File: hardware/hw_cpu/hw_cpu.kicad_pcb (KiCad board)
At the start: 2 copper layers, 85.7 x 40.6 mm, 60 parts, among them CON1 SD_Card, IC1 MT48LC4M16A2P, J1 USB_OTG, P1 COM_EXP, P2 IO_EXP, P3 DEBUG, Q1 BC849, SW1 RESET, U2 STM32F429ZGTx, Y1 8MHz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

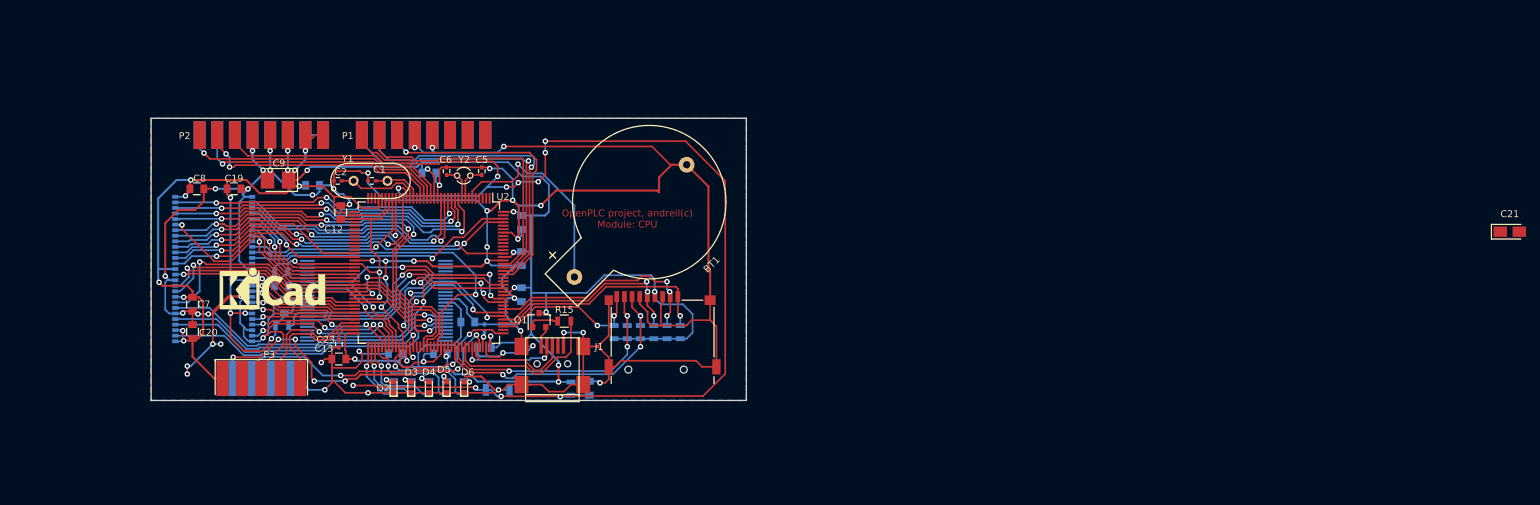
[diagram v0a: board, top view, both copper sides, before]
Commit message: Обновлена схема CPU
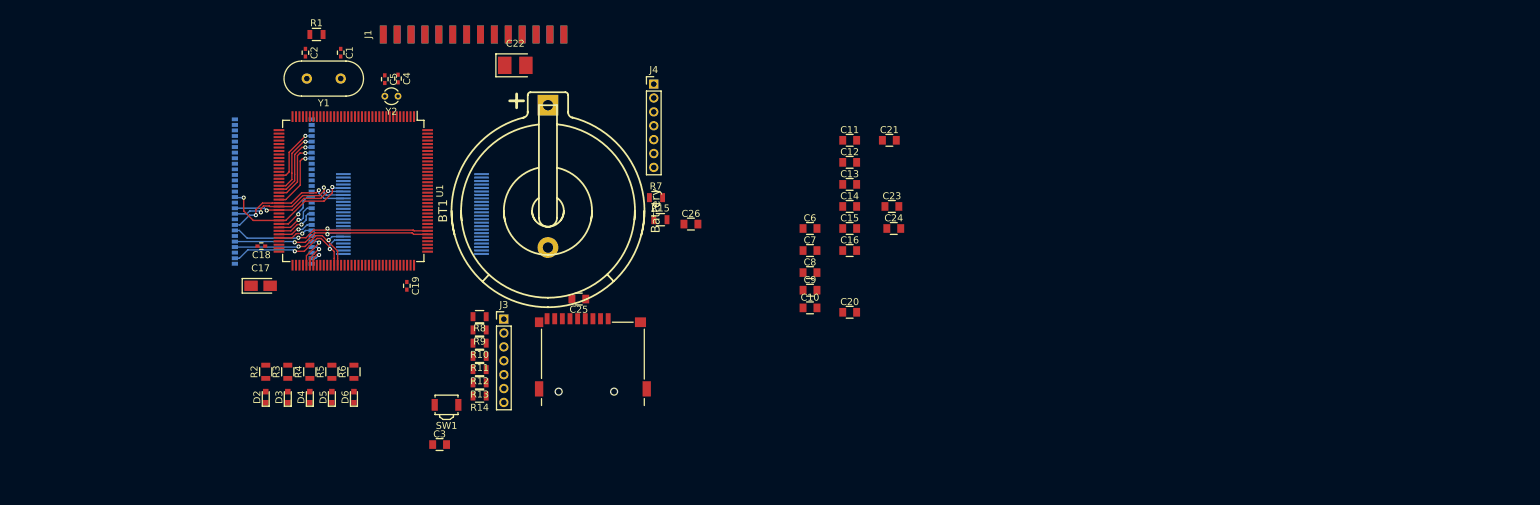
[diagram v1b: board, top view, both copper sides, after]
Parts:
- removed ??1: K9F5608, Housings_SSOP:TSOP-I-48_12x18.4mm_Pitch0.5mm
- removed P1: COM_EXP, andreil:IDC_Header_SMD_16pins
- removed P2: IO_EXP, andreil:IDC_Header_SMD_16pins
- removed P3: DEBUG, Connect:DB9F_CI
- removed Q1: BC849, TO_SOT_Packages_SMD:SOT-23
- removed REF***: KiCad-Logo_6mm_SilkScreen, Symbols:KiCad-Logo_6mm_SilkScreen
- removed the U2 at (114.3, 107.3)
- added J3: SDIO_DEB, Pin_Headers:Pin_Header_Straight_1x07_Pitch2.00mm, F.Cu at (125.1, 114.0)
- added J4: DEBUG, Pin_Headers:Pin_Header_Straight_1x07_Pitch2.00mm, F.Cu at (146.7, 80.2)
- added U1: STM32F429ZGTx, Housings_QFP:LQFP-144_20x20mm_Pitch0.5mm, F.Cu at (103.4, 95.6)
- added U3: K9F5608, Housings_SSOP:TSOP-I-48_12x18.4mm_Pitch0.5mm, B.Cu at (111.9, 98.9)
- BT1: footprint Connect:CR2032H -> w_battery_holders:keystone_1025
- C10, C11, C14, C15, C16, C24, C25, C26, C3, R1, R10, R11, R12, R13, R14, R2, R3, R4, R5, R6, R7, R8, R9, SW1: moved to F.Cu
- C17: value 100n -> 4,7u 10v; footprint Capacitors_SMD:C_0805 -> Capacitors_Tantalum_SMD:CP_Tantalum_Case-A_EIA-3216-18_Reflow; moved to F.Cu
- C18: value 100n -> 2,2u; footprint Capacitors_SMD:C_0805 -> Capacitors_SMD:C_0402; moved to F.Cu
- C19: value 100n -> 2,2u; footprint Capacitors_SMD:C_0805 -> Capacitors_SMD:C_0402
- C21: value 4,7u 10v -> 100n; footprint Capacitors_Tantalum_SMD:CP_Tantalum_Case-A_EIA-3216-18_Reflow -> Capacitors_SMD:C_0805
- C22: value 2,2u -> 4,7u 10v; footprint Capacitors_SMD:C_0402 -> Capacitors_Tantalum_SMD:CP_Tantalum_Case-B_EIA-3528-21_Reflow; moved to F.Cu
- C23: value 2,2u -> 100n; footprint Capacitors_SMD:C_0402 -> Capacitors_SMD:C_0805
- C4: value 100n -> 12p; footprint Capacitors_SMD:C_0805 -> Capacitors_SMD:C_0402; moved to F.Cu
- C6: value 12p -> 100n; footprint Capacitors_SMD:C_0402 -> Capacitors_SMD:C_0805
- C9: value 4,7u 10v -> 100n; footprint Capacitors_Tantalum_SMD:CP_Tantalum_Case-B_EIA-3528-21_Reflow -> Capacitors_SMD:C_0805
- J1: value USB_OTG -> CON_EXT; footprint Connect:USB_Mini-B -> Projects:Pin_Header_2.00mm_SMD
- J2: renamed from CON1; value SD_Card -> Micro_SD_Card_Det
- moved C20 94.7 mm to (174.9, 113.0), turned to 0 degrees
- moved C21 90.3 mm to (180.6, 88.3)
- moved C7 89.3 mm to (169.2, 104.1), turned to 0 degrees
- moved C8 89.1 mm to (169.2, 107.3)
- moved C24 88.6 mm to (181.2, 101.0)
- moved C23 82.0 mm to (181.0, 97.8), turned to 0 degrees
- moved C9 78.2 mm to (169.2, 109.9), turned to 0 degrees
- moved C16 77.9 mm to (174.9, 104.1)
- moved C13 77.7 mm to (174.9, 94.6), turned to 0 degrees
- moved C12 73.7 mm to (174.9, 91.4), turned to 0 degrees
- moved C14 68.8 mm to (174.9, 97.8), turned to 0 degrees
- moved R1 62.8 mm to (98.1, 73.0), turned to 0 degrees
- moved C15 61.6 mm to (174.9, 101.0), turned to 0 degrees
- moved R7 56.9 mm to (147.0, 96.5), turned to 0 degrees
- moved C6 53.0 mm to (169.2, 101.0), turned to 0 degrees
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- renumbered IC1 to U2
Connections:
- C18 pad 1: VREF -> VCAP1
- C19 pad 1: VREF -> VCAP2
- C22 pad 1: VCAP -> VREF
- C23 pad 1: VCAP -> VREF
- C24 pad 1: Net-(??1-Pad19) -> VREF
- C26 pad 1: VREF -> Net-(C26-Pad1)
- C4 pad 1: VREF -> BOOT0
- C4 pad 2: BOOT0 -> OSC32_IN
- C5 pad 2: OSC32_IN -> OSC32_OUT
- C6 pad 1: BOOT0 -> VREF
- C6 pad 2: OSC32_OUT -> BOOT0
- J1 pad 1: Net-(J1-Pad1) -> RESET
- J1 pad 2: USB_DM -> RESET
- J1 pad 3: USB_DP -> SPI_MISO
- J1 pad 4: Net-(J1-Pad4) -> SPI6_MISO
- J1 pad 5: BOOT0 -> SPI_MOSI
- J1 pad 6: BOOT0 -> SPI6_MOSI
- J2 pad 1: SDIO_D3 -> SDIO_D2
- J2 pad 2: SDIO_CMD -> SDIO_D3
- J2 pad 3: BOOT0 -> SDIO_CMD
- J2 pad 9: SDIO_D2 -> BOOT0
- R14 pad 1: VREF -> CARD_DET
- R14 pad 2: Net-(??1-Pad19) -> VREF
- R15 pad 1: Net-(Q1-Pad1) -> VREF
- R15 pad 2: USB_VBUS -> Net-(C26-Pad1)
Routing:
- net BOOT0: track 592.4 -> 0.00 mm, vias 51 -> 0
- net VREF: track 418.8 -> 0.00 mm, vias 31 -> 0
- net RESET: track 172.3 -> 0.00 mm, vias 11 -> 0
- net A15: track 60.0 -> 0.00 mm, vias 3 -> 0
- net A14: track 58.6 -> 0.00 mm, vias 3 -> 0
- net NBL0: track 52.1 -> 0.00 mm, vias 3 -> 0
- net SDNCAS: track 51.1 -> 0.00 mm, vias 3 -> 0
- net SWDIO: track 49.6 -> 0.00 mm, vias 7 -> 0
- net A0: track 49.1 -> 0.00 mm, vias 3 -> 0
- net SDCLK: track 48.0 -> 0.00 mm, vias 1 -> 0
- net A1: track 46.4 -> 0.00 mm, vias 3 -> 0
- net A2: track 45.3 -> 0.00 mm, vias 3 -> 0
- net SPI6_MISO: track 44.4 -> 0.00 mm, vias 1 -> 0
- net SPI6_SCK: track 44.3 -> 0.00 mm, vias 1 -> 0
- net A3: track 44.2 -> 0.00 mm, vias 3 -> 0
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- removed copper zone on B.Cu, net BOOT0
- removed copper zone on F.Cu, net BOOT0
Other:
- board outline removed
- net class Default: trace_width 0.25 -> 0.2; via_dia 0.8 -> 0.6; via_drill 0.4 -> 0.3
- board text removed: "OpenPLC project, andreil(c) Module: CPU"

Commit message: Обновлена плата CPU
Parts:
- moved U3 27.9 mm to (84.3, 95.6), turned to 90 degrees
- moved U2 11.4 mm to (103.3, 96.3), turned to 270 degrees
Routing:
- net D3: track 31.4 -> 0.00 mm, vias 2 -> 0
- net D2: track 31.1 -> 0.00 mm, vias 2 -> 0
- net A10: track 0.00 -> 24.0 mm, vias 0 -> 3
- net D0: track 21.6 -> 0.00 mm, vias 2 -> 0
- net A4: track 0.00 -> 21.4 mm, vias 0 -> 1
- net D1: track 21.3 -> 0.00 mm, vias 2 -> 0
- net A5: track 0.00 -> 21.1 mm, vias 0 -> 1
- net A15: track 0.00 -> 20.0 mm, vias 0 -> 3
- net A14: track 0.00 -> 19.9 mm, vias 0 -> 3
- net A3: track 0.00 -> 19.2 mm, vias 0 -> 1
- net NBL1: track 0.00 -> 19.0 mm, vias 0 -> 1
- net BOOT0: track 0.00 -> 15.7 mm, vias 0 -> 1
- net A2: track 0.00 -> 15.7 mm, vias 0 -> 1
- net A6: track 8.73 -> 22.7 mm
- net A1: track 0.00 -> 13.4 mm, vias 0 -> 1
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
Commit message: Обновлена плата CPU
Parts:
- moved J3 35.5 mm to (160.6, 114.7)
- moved R14 34.5 mm to (156.1, 127.0)
- moved R9 33.6 mm to (155.1, 117.9)
- moved R10 30.4 mm to (151.8, 121.2)
- moved R12 30.4 mm to (151.5, 126.5)
- moved R8 28.3 mm to (149.8, 111.8)
- moved R11 27.1 mm to (148.7, 120.1)
- moved U3 26.9 mm to (103.4, 114.4), turned to 180 degrees
- moved R13 26.5 mm to (147.9, 126.7)
- moved J2 9.21 mm to (128.9, 126.4)
- moved C17 4.97 mm to (85.9, 112.0)
- moved U2 0.74 mm to (103.7, 95.6), turned to 0 degrees
- moved C4 0.11 mm to (109.9, 79.5)
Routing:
- net NBL0: track 0.00 -> 21.2 mm, vias 0 -> 1
- net D3: track 0.00 -> 18.4 mm, vias 0 -> 1
- net D2: track 0.00 -> 17.9 mm, vias 0 -> 1
- net A4: track 21.4 -> 5.04 mm
- net SDCKE0: track 0.00 -> 16.4 mm, vias 0 -> 1
- net BOOT0: track 15.7 -> 0.00 mm, vias 1 -> 0
- net A5: track 21.1 -> 6.29 mm
- net A10: track 24.0 -> 11.0 mm, vias 3 -> 1
- net SDCLK: track 4.90 -> 16.6 mm
- net OSC_OUT: track 0.00 -> 11.7 mm
- net D12: track 5.74 -> 17.0 mm
- net SDNWE: track 0.00 -> 10.7 mm, vias 0 -> 1
- net D13: track 4.68 -> 15.3 mm
- net D11: track 6.80 -> 17.1 mm
- net D6: track 14.8 -> 5.57 mm
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
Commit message: Обновлена плата CPU
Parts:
- added REF**: MountingHole_2.2mm_M2_Pad, Mounting_Holes:MountingHole_2.2mm_M2_Pad, F.Cu at (139.7, 74.9)
- added REF**: MountingHole_2.2mm_M2_Pad, Mounting_Holes:MountingHole_2.2mm_M2_Pad, F.Cu at (104.8, 74.3)
- added REF**: MountingHole_3.2mm_M3, Mounting_Holes:MountingHole_3.2mm_M3, F.Cu at (139.1, 82.5)
- added REF**: MountingHole_3.2mm_M3, Mounting_Holes:MountingHole_3.2mm_M3, F.Cu at (139.1, 110.5)
- added REF**: MountingHole_3.2mm_M3, Mounting_Holes:MountingHole_3.2mm_M3, F.Cu at (60.3, 82.5)
- added REF**: MountingHole_3.2mm_M3, Mounting_Holes:MountingHole_3.2mm_M3, F.Cu at (60.3, 114.3)
- C25, C26, C3, R1, R10, R11, R12, R13, R15, R8, R9, SW1: moved to B.Cu
- J4: value DEBUG -> PROG; footprint Pin_Headers:Pin_Header_Straight_1x07_Pitch2.00mm -> Connect:DB9MD
- moved J4 88.5 mm to (69.2, 122.9)
- moved BT1 57.2 mm to (74.3, 101.6)
- moved C26 38.9 mm to (116.8, 116.8), turned to 90 degrees
- moved C10 37.7 mm to (133.5, 100.1)
- moved C11 37.7 mm to (139.2, 76.0)
- moved C12 37.7 mm to (139.2, 79.2)
- moved C13 37.7 mm to (139.2, 82.4)
- moved C14 37.7 mm to (139.2, 85.5)
- moved C15 37.7 mm to (139.2, 88.7)
- moved C16 37.7 mm to (139.2, 91.9)
- moved C20 37.7 mm to (139.2, 100.8)
- moved C21 37.7 mm to (144.9, 76.0)
- moved C24 37.7 mm to (145.6, 88.7)
- moved C6 37.7 mm to (133.5, 88.7)
- moved C7 37.7 mm to (133.5, 91.9)
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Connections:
- J3 pad 1: SDIO_D0 -> SDIO_D2
- J3 pad 2: SDIO_D1 -> SDIO_D3
- J3 pad 3: SDIO_D2 -> SDIO_CMD
- J3 pad 4: SDIO_D3 -> SDIO_CK
- J3 pad 5: SDIO_CMD -> SDIO_D0
- J3 pad 6: SDIO_CK -> SDIO_D1
- J4 pad 1: SWDIO -> UART_RX
- J4 pad 2: SWCLK -> UART_TX
- J4 pad 3: RESET -> BOOT0
- J4 pad 4: VREF -> Net-(J4-Pad4)
- J4 pad 5: BOOT0 -> VREF
- J4 pad 6: UART_TX -> BOOT0
- J4 pad 7: UART_RX -> RESET
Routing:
- net SWCLK: track 0.00 -> 50.6 mm, vias 0 -> 2
- net SWDIO: track 0.00 -> 46.8 mm, vias 0 -> 2
- net UART_RX: track 0.00 -> 36.1 mm
- net SDIO_D2: track 0.00 -> 32.0 mm, vias 0 -> 2
- net UART_TX: track 0.00 -> 30.9 mm
- net SDIO_D3: track 0.00 -> 30.3 mm, vias 0 -> 2
- net SDIO_D0: track 0.00 -> 29.6 mm, vias 0 -> 1
- net SDIO_CMD: track 0.00 -> 29.1 mm
- net SDIO_CK: track 0.00 -> 27.2 mm
- net SDIO_D1: track 0.00 -> 25.8 mm
- net NWE: track 0.00 -> 24.2 mm, vias 0 -> 3
- net LED5: track 0.00 -> 22.0 mm, vias 0 -> 2
- net SPI_SCK: track 0.00 -> 21.9 mm, vias 0 -> 2
- net A16: track 0.00 -> 20.9 mm, vias 0 -> 1
- net A17: track 0.00 -> 20.6 mm, vias 0 -> 1
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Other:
- board outline added: 89.5 x 59.7 mm

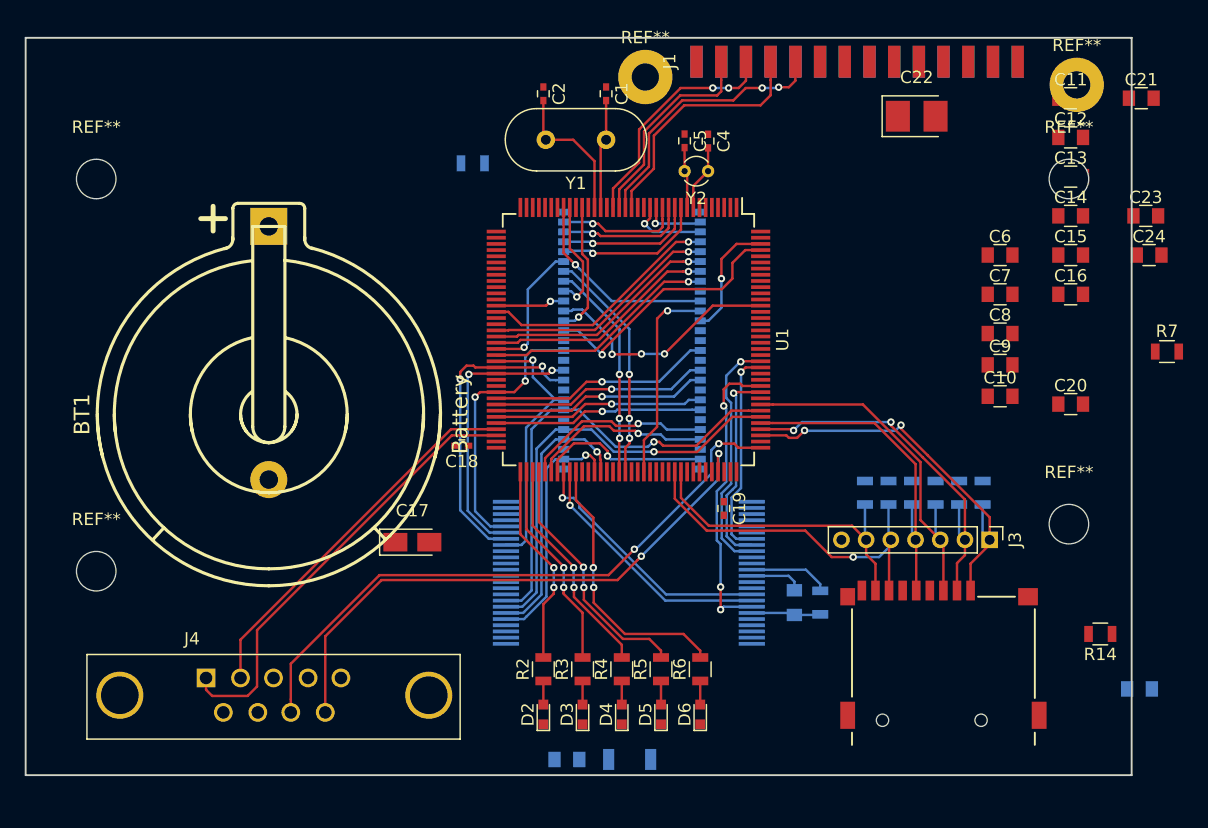
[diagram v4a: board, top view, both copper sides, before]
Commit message: Обновлены схема и плата CPU.
Добавлены переключатель START/STOP, кнопки DUMP и RESTORE.
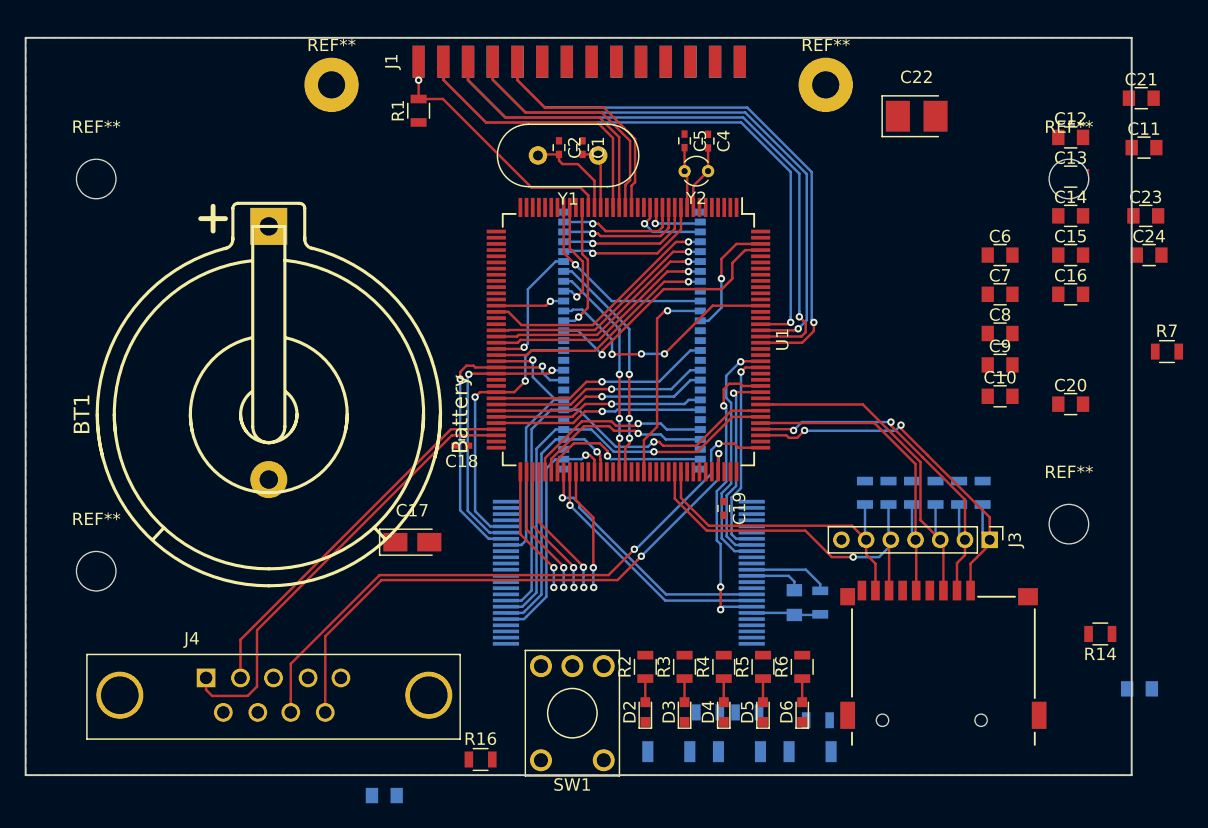
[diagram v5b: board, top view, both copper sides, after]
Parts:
- added R16: 10k, Resistors_SMD:R_0805, F.Cu at (91.4, 129.5)
- added R17: 10k, Resistors_SMD:R_0805, B.Cu at (109.9, 125.7)
- added R18: 10k, Resistors_SMD:R_0805, B.Cu at (118.7, 126.4)
- added R19: 10k, Resistors_SMD:R_0805, B.Cu at (113.0, 125.7)
- added SW2: RESTORE, Buttons_Switches_SMD:SW_SPST_B3U-3000P, B.Cu at (118.1, 128.9)
- added SW3: DUMP, Buttons_Switches_SMD:SW_SPST_B3U-3000P, B.Cu at (112.4, 128.9)
- added SW4: RESET, Buttons_Switches_SMD:SW_SPST_B3U-3000P, B.Cu at (106.7, 128.9)
- R1: moved to F.Cu
- SW1: value RESET -> RUN/STOP; footprint Buttons_Switches_SMD:SW_SPST_B3U-3000P -> Buttons_Switches_ThroughHole:KSA_Tactile_SPST; moved to F.Cu
- moved REF** 25.4 mm to (79.4, 74.9)
- moved J1 22.5 mm to (99.4, 73.0)
- moved REF** 20.3 mm to (119.4, 74.9)
- moved C3 15.1 mm to (83.6, 132.5)
- moved D2 8.26 mm to (104.8, 125.7)
- moved D3 8.26 mm to (108.0, 125.7)
- moved R2 8.26 mm to (104.8, 122.0)
- moved R3 8.26 mm to (108.0, 122.0)
- moved D4 8.26 mm to (111.1, 125.7)
- moved D5 8.26 mm to (114.3, 125.7)
- moved D6 8.26 mm to (117.5, 125.7)
- moved R4 8.26 mm to (111.1, 122.0)
- moved R5 8.26 mm to (114.3, 122.0)
- moved R6 8.26 mm to (117.5, 122.0)
- moved C11 7.16 mm to (145.1, 80.0)
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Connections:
- J1 pad 10: SPI6_SCK -> SPI6_SEL
- J1 pad 3: SPI_MISO -> SPI_MOSI
- J1 pad 4: SPI6_MISO -> SPI6_MOSI
- J1 pad 5: SPI_MOSI -> SPI_MISO
- J1 pad 6: SPI6_MOSI -> SPI6_MISO
- J1 pad 7: SPI_SEL -> SPI_SCK
- J1 pad 8: SPI6_SEL -> SPI6_SCK
- J1 pad 9: SPI_SCK -> SPI_SEL
- SW1 pad 1: RESET -> RUN
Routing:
- net SPI6_MISO: track 0.00 -> 48.3 mm, vias 0 -> 1
- net SPI6_MOSI: track 0.00 -> 47.3 mm, vias 0 -> 1
- net SPI6_SEL: track 0.00 -> 46.0 mm, vias 0 -> 1
- net SPI6_SCK: track 0.00 -> 46.0 mm, vias 0 -> 1
- net RESET: track 0.00 -> 22.5 mm, vias 0 -> 1
- net LED5: track 22.0 -> 9.96 mm
- net LED4: track 20.4 -> 10.9 mm
- net LED3: track 18.0 -> 10.7 mm
- net LED2: track 16.9 -> 10.6 mm
- net LED1: track 16.5 -> 10.5 mm
- net SPI_MISO: track 17.0 -> 21.3 mm
- net SPI_MOSI: track 19.0 -> 22.8 mm, vias 2 -> 0
- net OSC_OUT: track 11.7 -> 7.95 mm
- net OSC_IN: track 8.84 -> 5.60 mm
- net SPI_SCK: track 21.9 -> 20.2 mm, vias 2 -> 0
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- added copper zone on B.Cu, net BOOT0
- added copper zone on F.Cu, net BOOT0
